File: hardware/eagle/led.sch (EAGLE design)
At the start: 15 parts, among them IC1 MCP1406SOIC8, IC10 MCP1406SOIC8, IC11 MCP1406SOIC8, IC12 MCP1406SOIC8, IC13 MCP2551SOIC8, IC2 MCP1406SOIC8, IC3 MCP1406SOIC8, IC4 MCP1406SOIC8, IC5 MCP1406SOIC8, IC6 MCP1406SOIC8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

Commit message: neue boaerd version + datasheets added
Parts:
- removed JP2: (no value), pinhead:PINHD-2X13
- added C2: (no value), rcl:CPOL-EUE5-10.5
- added EXT1: (no value), pinhead:PINHD-2X13
- added IC14: 7805T, linear:7805T
- added U$1, U$10, U$11, U$2, U$3, U$5, U$6, U$7, U$8, U$9: 2KLEMME, custom-parts:2KLEMME
- renumbered JP1 to EXT2
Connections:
- new net B1: EXT1.17, IC1.INPUT
- new net B2: EXT1.26, IC4.INPUT
- new net B3: EXT1.16, IC7.INPUT
- new net B4: EXT2.10, IC10.INPUT
- new net CANH: IC13.CANH, U$3.1
- new net CANL: IC13.CANL, U$3.2
- new net CANRX: EXT1.1, IC13.RXD
- new net CANTX: EXT1.3, IC13.TXD
- new net G1: EXT1.15, IC2.INPUT
- new net G2: EXT1.22, IC5.INPUT
- new net G3: EXT2.7, IC8.INPUT
- new net G4: EXT2.8, IC11.INPUT
- new net N$10: IC8.OUT1, IC8.OUT2, U$8.2
- new net N$11: IC7.OUT1, IC7.OUT2, U$7.1
- new net N$12: IC12.OUT1, IC12.OUT2, U$9.1
- new net N$13: IC11.OUT1, IC11.OUT2, U$9.2
- new net N$14: IC10.OUT1, IC10.OUT2, U$2.1
- new net N$2: C2.-, IC14.GND, U$1.2
- new net N$3: IC3.OUT1, IC3.OUT2, U$5.1
- new net N$4: IC2.OUT1, IC2.OUT2, U$5.2
- new net N$5: IC1.OUT1, IC1.OUT2, U$6.1
- new net N$6: IC6.OUT1, IC6.OUT2, U$10.1
- new net N$7: IC5.OUT1, IC5.OUT2, U$10.2
- new net N$8: IC4.OUT1, IC4.OUT2, U$11.1
- new net N$9: IC9.OUT1, IC9.OUT2, U$8.1
- new net R1: EXT1.13, IC3.INPUT
- new net R2: EXT1.21, IC6.INPUT
- new net R3: EXT1.14, IC9.INPUT
- new net R4: EXT2.4, IC12.INPUT
- new net VCC: EXT2.26, IC13.VDD, IC14.VO
- net +12V: now also C2.+, IC14.VI, U$1.1, U$2.2
- net GND: now also EXT2.25, IC13.GND, U$11.2, U$6.2, U$7.2

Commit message: hardware changed
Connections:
- net +12V: no longer U$2.2
- net B3: now also EXT1.14; no longer EXT1.16
- net G3: now also EXT1.16; no longer EXT2.7
- net GND: now also U$2.2
- net R3: now also EXT2.7; no longer EXT1.14
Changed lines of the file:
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@@
 <pinref part="GND5" gate="1" pin="GND"/>
 <wire x1="241.3" y1="55.88" x2="246.38" y2="55.88" width="0.1524" layer="91"/>
-<wire x1="246.38" y1="55.88" x2="246.38" y2="38.1" width="0.1524" layer="91"/>
+<wire x1="246.38" y1="55.88" x2="246.38" y2="50.8" width="0.1524" layer="91"/>
 <pinref part="IC10" gate="G$1" pin="GND2"/>
+<wire x1="246.38" y1="50.8" x2="246.38" y2="38.1" width="0.1524" layer="91"/>
 <wire x1="246.38" y1="38.1" x2="246.38" y2="20.32" width="0.1524" layer="91"/>
 <wire x1="246.38" y1="20.32" x2="246.38" y2="12.7" width="0.1524" layer="91"/>
@@
 <junction x="246.38" y="38.1"/>
 <junction x="246.38" y="55.88"/>
+<pinref part="U$2" gate="G$1" pin="2"/>
+<wire x1="279.4" y1="86.36" x2="279.4" y2="50.8" width="0.1524" layer="91"/>
+<wire x1="279.4" y1="50.8" x2="246.38" y2="50.8" width="0.1524" layer="91"/>
+<junction x="246.38" y="50.8"/>
 </segment>
 <segment>
@@
 <junction x="256.54" y="63.5"/>
 <junction x="256.54" y="27.94"/>
-<pinref part="U$2" gate="G$1" pin="2"/>
-<wire x1="279.4" y1="86.36" x2="279.4" y2="45.72" width="0.1524" layer="91"/>
-<wire x1="279.4" y1="45.72" x2="256.54" y2="45.72" width="0.1524" layer="91"/>
 </segment>
 <segment>
@@
 <pinref part="IC9" gate="G$1" pin="INPUT"/>
 <wire x1="144.78" y1="60.96" x2="142.24" y2="60.96" width="0.1524" layer="91"/>
-<label x="139.7" y="58.42" size="1.778" layer="95"/>
+<label x="137.16" y="60.96" size="1.778" layer="95"/>
+</segment>
+<segment>
+<pinref part="EXT2" gate="A" pin="7"/>
+<wire x1="353.06" y1="137.16" x2="342.9" y2="137.16" width="0.1524" layer="91"/>
+<label x="337.82" y="137.16" size="1.778" layer="95"/>
+</segment>
+</net>
+<net name="G3" class="0">
+<segment>
+<pinref part="IC8" gate="G$1" pin="INPUT"/>
+<wire x1="144.78" y1="43.18" x2="142.24" y2="43.18" width="0.1524" layer="91"/>
+<label x="134.62" y="43.18" size="1.778" layer="95"/>
+</segment>
+<segment>
+<pinref part="EXT1" gate="A" pin="16"/>
+<wire x1="302.26" y1="127" x2="312.42" y2="127" width="0.1524" layer="91"/>
+<label x="314.96" y="127" size="1.778" layer="95"/>
+</segment>
+</net>
+<net name="B3" class="0">
+<segment>
+<pinref part="IC7" gate="G$1" pin="INPUT"/>
+<wire x1="144.78" y1="25.4" x2="142.24" y2="25.4" width="0.1524" layer="91"/>
+<label x="134.62" y="25.4" size="1.778" layer="95"/>
 </segment>
 <segment>
@@
 </segment>
 </net>
-<net name="G3" class="0">
-<segment>
-<pinref part="IC8" gate="G$1" pin="INPUT"/>
-<wire x1="144.78" y1="43.18" x2="142.24" y2="43.18" width="0.1524" layer="91"/>
-<label x="132.08" y="40.64" size="1.778" layer="95"/>
-</segment>
-<segment>
-<pinref part="EXT2" gate="A" pin="7"/>
-<wire x1="353.06" y1="137.16" x2="342.9" y2="137.16" width="0.1524" layer="91"/>
-<label x="337.82" y="137.16" size="1.778" layer="95"/>
-</segment>
-</net>
-<net name="B3" class="0">
-<segment>
-<pinref part="IC7" gate="G$1" pin="INPUT"/>
-<wire x1="144.78" y1="25.4" x2="142.24" y2="25.4" width="0.1524" layer="91"/>
-<label x="134.62" y="22.86" size="1.778" layer="95"/>
-</segment>
-<segment>
-<pinref part="EXT1" gate="A" pin="16"/>
-<wire x1="302.26" y1="127" x2="312.42" y2="127" width="0.1524" layer="91"/>
-<label x="314.96" y="127" size="1.778" layer="95"/>
-</segment>
-</net>

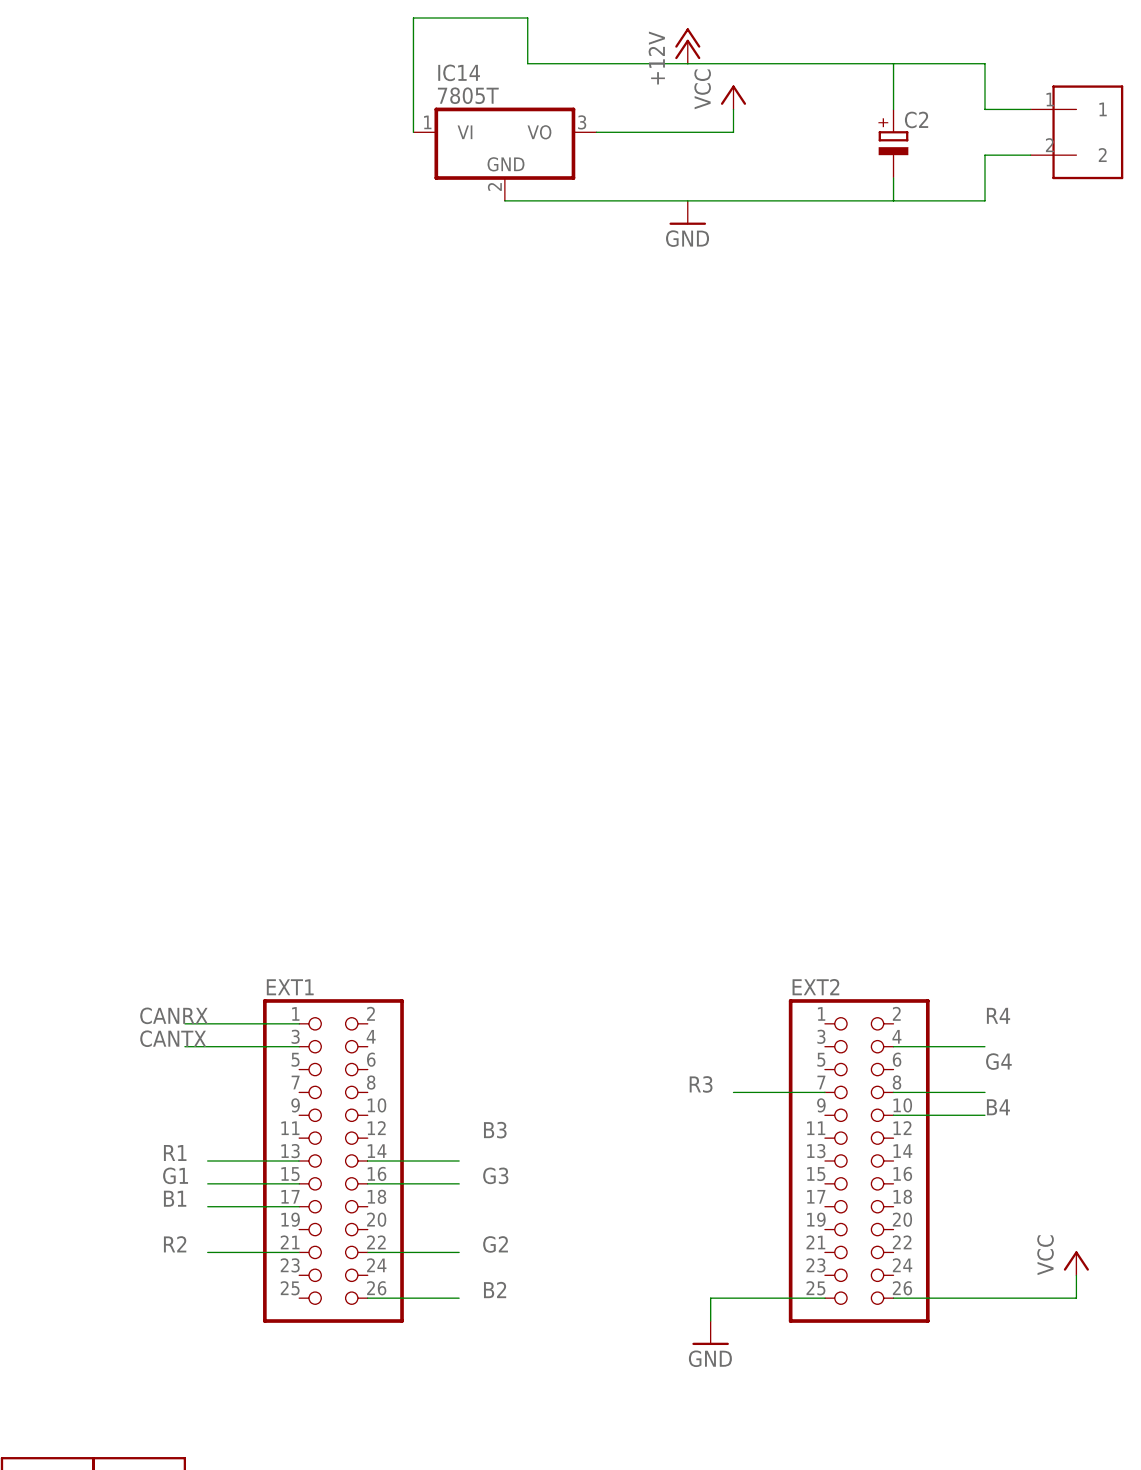
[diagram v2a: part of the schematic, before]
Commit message: neues board nicht fertig geroutet wegen kreuzungen
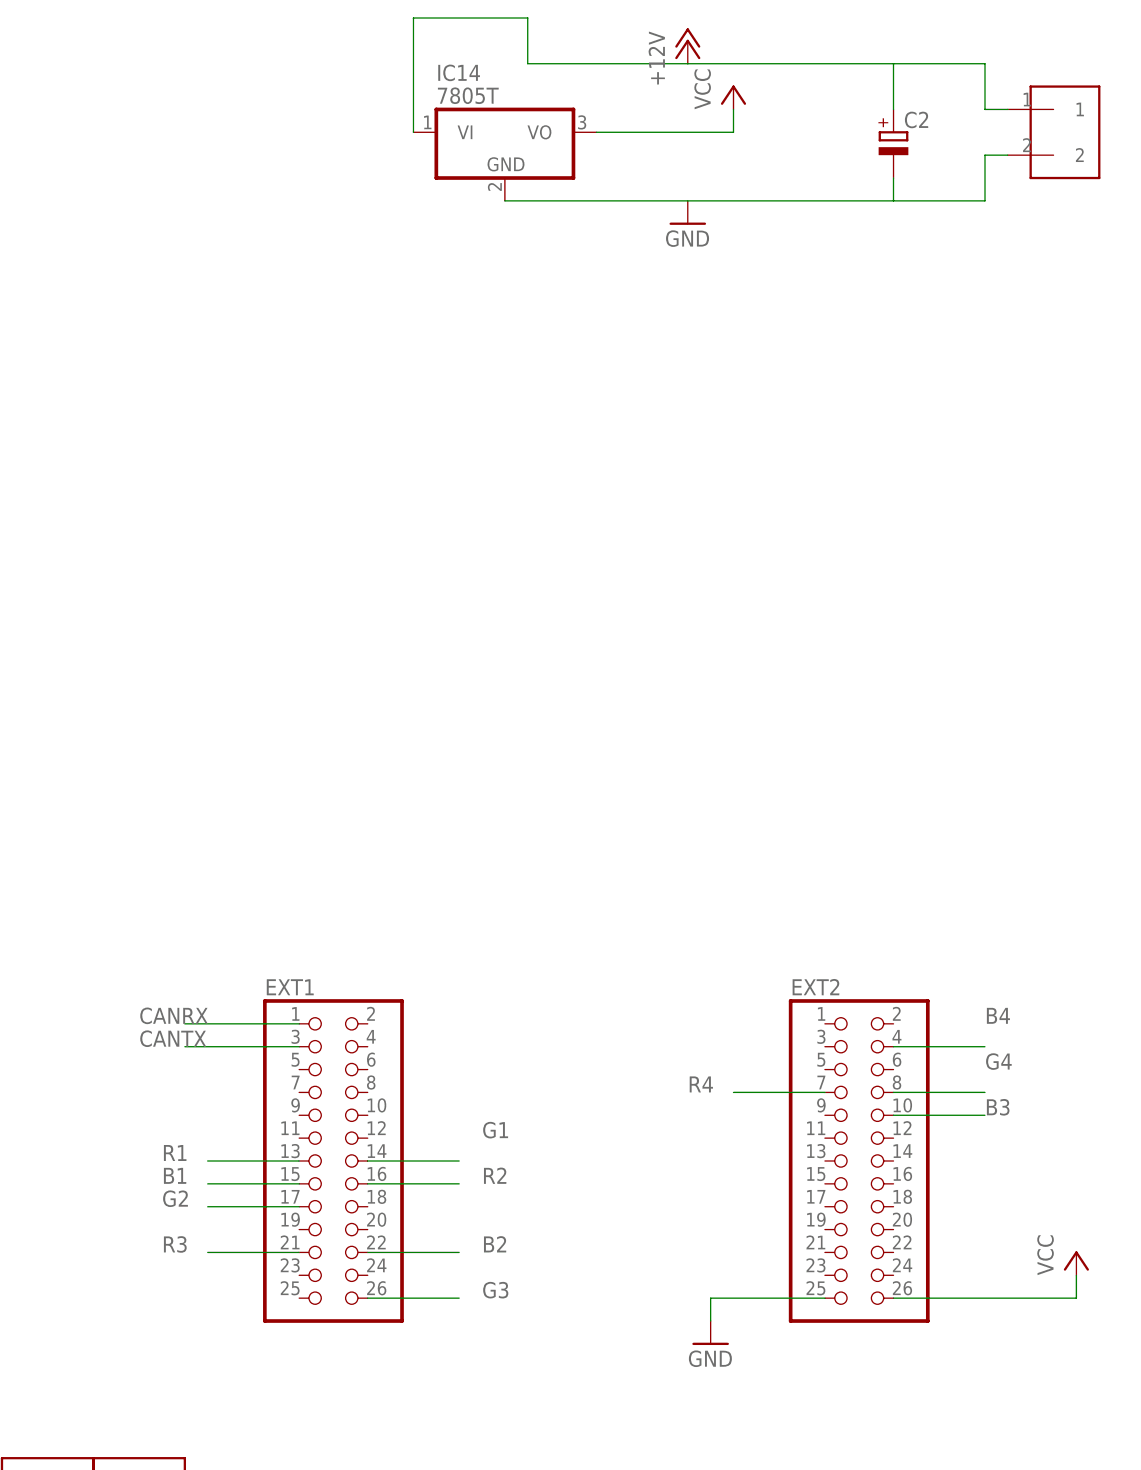
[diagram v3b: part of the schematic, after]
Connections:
- net B1: now also EXT1.15; no longer EXT1.17
- net B2: now also EXT1.22; no longer EXT1.26
- net B3: now also EXT2.10; no longer EXT1.14
- net B4: now also EXT2.4; no longer EXT2.10
- net G1: now also EXT1.14; no longer EXT1.15
- net G2: now also EXT1.17; no longer EXT1.22
- net G3: now also EXT1.26; no longer EXT1.16
- net R2: now also EXT1.16; no longer EXT1.21
- net R3: now also EXT1.21; no longer EXT2.7
- net R4: now also EXT2.7; no longer EXT2.4
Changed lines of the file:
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@@
 <instance part="P+6" gate="1" x="337.82" y="254"/>
 <instance part="GND6" gate="1" x="337.82" y="233.68"/>
-<instance part="U$1" gate="G$1" x="383.54" y="243.84"/>
+<instance part="U$1" gate="G$1" x="381" y="243.84"/>
 <instance part="U$2" gate="G$1" x="276.86" y="93.98" rot="R90"/>
 <instance part="U$5" gate="G$1" x="60.96" y="93.98" rot="R90"/>
@@
 <wire x1="360.68" y1="251.46" x2="370.84" y2="251.46" width="0.1524" layer="91"/>
 <wire x1="360.68" y1="251.46" x2="360.68" y2="246.38" width="0.1524" layer="91"/>
-<pinref part="U$1" gate="G$1" pin="1"/>
-<wire x1="375.92" y1="246.38" x2="370.84" y2="246.38" width="0.1524" layer="91"/>
 <wire x1="370.84" y1="246.38" x2="370.84" y2="251.46" width="0.1524" layer="91"/>
 <wire x1="337.82" y1="251.46" x2="320.04" y2="251.46" width="0.1524" layer="91"/>
@@
 <wire x1="320.04" y1="256.54" x2="307.34" y2="256.54" width="0.1524" layer="91"/>
 <wire x1="307.34" y1="256.54" x2="307.34" y2="243.84" width="0.1524" layer="91"/>
+<pinref part="U$1" gate="G$1" pin="1"/>
+<wire x1="373.38" y1="246.38" x2="370.84" y2="246.38" width="0.1524" layer="91"/>
 </segment>
 </net>
@@
 <wire x1="360.68" y1="236.22" x2="370.84" y2="236.22" width="0.1524" layer="91"/>
 <wire x1="360.68" y1="238.76" x2="360.68" y2="236.22" width="0.1524" layer="91"/>
-<pinref part="U$1" gate="G$1" pin="2"/>
-<wire x1="375.92" y1="241.3" x2="370.84" y2="241.3" width="0.1524" layer="91"/>
 <wire x1="370.84" y1="241.3" x2="370.84" y2="236.22" width="0.1524" layer="91"/>
 <pinref part="IC14" gate="A1" pin="GND"/>
+<pinref part="U$1" gate="G$1" pin="2"/>
+<wire x1="373.38" y1="241.3" x2="370.84" y2="241.3" width="0.1524" layer="91"/>
 </segment>
 </net>
@@
 </segment>
 <segment>
+<pinref part="EXT1" gate="A" pin="14"/>
+<wire x1="302.26" y1="129.54" x2="312.42" y2="129.54" width="0.1524" layer="91"/>
+<label x="314.96" y="132.08" size="1.778" layer="95"/>
+</segment>
+</net>
+<net name="B1" class="0">
+<segment>
+<pinref part="IC1" gate="G$1" pin="INPUT"/>
+<wire x1="22.86" y1="25.4" x2="20.32" y2="25.4" width="0.1524" layer="91"/>
+<label x="10.16" y="22.86" size="1.778" layer="95"/>
+</segment>
+<segment>
 <pinref part="EXT1" gate="A" pin="15"/>
 <wire x1="294.64" y1="127" x2="284.48" y2="127" width="0.1524" layer="91"/>
@@
 </segment>
 </net>
-<net name="B1" class="0">
-<segment>
-<pinref part="IC1" gate="G$1" pin="INPUT"/>
-<wire x1="22.86" y1="25.4" x2="20.32" y2="25.4" width="0.1524" layer="91"/>
-<label x="10.16" y="22.86" size="1.778" layer="95"/>
+<net name="B2" class="0">
+<segment>
+<pinref part="IC4" gate="G$1" pin="INPUT"/>
+<wire x1="83.82" y1="25.4" x2="81.28" y2="25.4" width="0.1524" layer="91"/>
+<label x="71.12" y="22.86" size="1.778" layer="95"/>
+</segment>
+<segment>
+<pinref part="EXT1" gate="A" pin="22"/>
+<wire x1="302.26" y1="119.38" x2="312.42" y2="119.38" width="0.1524" layer="91"/>
+<label x="314.96" y="119.38" size="1.778" layer="95"/>
+</segment>
+</net>
+<net name="G2" class="0">
+<segment>
+<pinref part="IC5" gate="G$1" pin="INPUT"/>
+<wire x1="83.82" y1="43.18" x2="81.28" y2="43.18" width="0.1524" layer="91"/>
+<label x="71.12" y="40.64" size="1.778" layer="95"/>
 </segment>
 <segment>
@@
 </segment>
 </net>
-<net name="B2" class="0">
-<segment>
-<pinref part="IC4" gate="G$1" pin="INPUT"/>
-<wire x1="83.82" y1="25.4" x2="81.28" y2="25.4" width="0.1524" layer="91"/>
-<label x="71.12" y="22.86" size="1.778" layer="95"/>
+<net name="R3" class="0">
+<segment>
+<pinref part="IC9" gate="G$1" pin="INPUT"/>
+<wire x1="144.78" y1="60.96" x2="142.24" y2="60.96" width="0.1524" layer="91"/>
+<label x="137.16" y="60.96" size="1.778" layer="95"/>
+</segment>
+<segment>
+<pinref part="EXT1" gate="A" pin="21"/>
+<wire x1="294.64" y1="119.38" x2="284.48" y2="119.38" width="0.1524" layer="91"/>
+<label x="279.4" y="119.38" size="1.778" layer="95"/>
+</segment>
+</net>
+<net name="G3" class="0">
+<segment>
+<pinref part="IC8" gate="G$1" pin="INPUT"/>
+<wire x1="144.78" y1="43.18" x2="142.24" y2="43.18" width="0.1524" layer="91"/>
+<label x="134.62" y="43.18" size="1.778" layer="95"/>
 </segment>
 <segment>
@@
 </segment>
 </net>
-<net name="G2" class="0">
-<segment>
-<pinref part="IC5" gate="G$1" pin="INPUT"/>
-<wire x1="83.82" y1="43.18" x2="81.28" y2="43.18" width="0.1524" layer="91"/>
-<label x="71.12" y="40.64" size="1.778" layer="95"/>
-</segment>
-<segment>
-<pinref part="EXT1" gate="A" pin="22"/>
-<wire x1="302.26" y1="119.38" x2="312.42" y2="119.38" width="0.1524" layer="91"/>
-<label x="314.96" y="119.38" size="1.778" layer="95"/>
-</segment>
-</net>
-<net name="R3" class="0">
-<segment>
-<pinref part="IC9" gate="G$1" pin="INPUT"/>
-<wire x1="144.78" y1="60.96" x2="142.24" y2="60.96" width="0.1524" layer="91"/>
-<label x="137.16" y="60.96" size="1.778" layer="95"/>
+<net name="B3" class="0">
+<segment>
+<pinref part="IC7" gate="G$1" pin="INPUT"/>
+<wire x1="144.78" y1="25.4" x2="142.24" y2="25.4" width="0.1524" layer="91"/>
+<label x="134.62" y="25.4" size="1.778" layer="95"/>
+</segment>
+<segment>
+<pinref part="EXT2" gate="A" pin="10"/>
+<wire x1="360.68" y1="134.62" x2="370.84" y2="134.62" width="0.1524" layer="91"/>
+<label x="370.84" y="134.62" size="1.778" layer="95"/>
+</segment>
+</net>
+<net name="B4" class="0">
+<segment>
+<pinref part="IC10" gate="G$1" pin="INPUT"/>
+<wire x1="210.82" y1="25.4" x2="208.28" y2="25.4" width="0.1524" layer="91"/>
+<label x="198.12" y="22.86" size="1.778" layer="95"/>
+</segment>
+<segment>
+<pinref part="EXT2" gate="A" pin="4"/>
+<wire x1="360.68" y1="142.24" x2="370.84" y2="142.24" width="0.1524" layer="91"/>
+<label x="370.84" y="144.78" size="1.778" layer="95"/>
+</segment>
+</net>
+<net name="G4" class="0">
+<segment>
+<pinref part="IC11" gate="G$1" pin="INPUT"/>
+<wire x1="210.82" y1="43.18" x2="208.28" y2="43.18" width="0.1524" layer="91"/>
+<label x="198.12" y="40.64" size="1.778" layer="95"/>
+</segment>
+<segment>
+<pinref part="EXT2" gate="A" pin="8"/>
+<wire x1="360.68" y1="137.16" x2="370.84" y2="137.16" width="0.1524" layer="91"/>
+<label x="370.84" y="139.7" size="1.778" layer="95"/>
+</segment>
+</net>
+<net name="R4" class="0">
+<segment>
+<pinref part="IC12" gate="G$1" pin="INPUT"/>
+<wire x1="210.82" y1="60.96" x2="208.28" y2="60.96" width="0.1524" layer="91"/>
+<label x="203.2" y="58.42" size="1.778" layer="95"/>
 </segment>
 <segment>
@@
 </segment>
 </net>
-<net name="G3" class="0">
-<segment>
-<pinref part="IC8" gate="G$1" pin="INPUT"/>
-<wire x1="144.78" y1="43.18" x2="142.24" y2="43.18" width="0.1524" layer="91"/>
-<label x="134.62" y="43.18" size="1.778" layer="95"/>
+<net name="R2" class="0">
+<segment>
+<pinref part="IC6" gate="G$1" pin="INPUT"/>
+<wire x1="83.82" y1="60.96" x2="81.28" y2="60.96" width="0.1524" layer="91"/>
+<label x="76.2" y="58.42" size="1.778" layer="95"/>
 </segment>
 <segment>
@@
 </segment>
 </net>
-<net name="B3" class="0">
-<segment>
-<pinref part="IC7" gate="G$1" pin="INPUT"/>
-<wire x1="144.78" y1="25.4" x2="142.24" y2="25.4" width="0.1524" layer="91"/>
-<label x="134.62" y="25.4" size="1.778" layer="95"/>
-</segment>
-<segment>
-<pinref part="EXT1" gate="A" pin="14"/>
-<wire x1="302.26" y1="129.54" x2="312.42" y2="129.54" width="0.1524" layer="91"/>
-<label x="314.96" y="132.08" size="1.778" layer="95"/>
-</segment>
-</net>
-<net name="B4" class="0">
-<segment>
-<pinref part="IC10" gate="G$1" pin="INPUT"/>
-<wire x1="210.82" y1="25.4" x2="208.28" y2="25.4" width="0.1524" layer="91"/>
-<label x="198.12" y="22.86" size="1.778" layer="95"/>
-</segment>
-<segment>
-<pinref part="EXT2" gate="A" pin="10"/>
-<wire x1="360.68" y1="134.62" x2="370.84" y2="134.62" width="0.1524" layer="91"/>
-<label x="370.84" y="134.62" size="1.778" layer="95"/>
-</segment>
-</net>
-<net name="G4" class="0">
-<segment>
-<pinref part="IC11" gate="G$1" pin="INPUT"/>
-<wire x1="210.82" y1="43.18" x2="208.28" y2="43.18" width="0.1524" layer="91"/>
-<label x="198.12" y="40.64" size="1.778" layer="95"/>
-</segment>
-<segment>
-<pinref part="EXT2" gate="A" pin="8"/>
-<wire x1="360.68" y1="137.16" x2="370.84" y2="137.16" width="0.1524" layer="91"/>
-<label x="370.84" y="139.7" size="1.778" layer="95"/>
-</segment>
-</net>
-<net name="R4" class="0">
-<segment>
-<pinref part="IC12" gate="G$1" pin="INPUT"/>
-<wire x1="210.82" y1="60.96" x2="208.28" y2="60.96" width="0.1524" layer="91"/>
-<label x="203.2" y="58.42" size="1.778" layer="95"/>
-</segment>
-<segment>
-<pinref part="EXT2" gate="A" pin="4"/>
-<wire x1="360.68" y1="142.24" x2="370.84" y2="142.24" width="0.1524" layer="91"/>
-<label x="370.84" y="144.78" size="1.778" layer="95"/>
-</segment>
-</net>
-<net name="R2" class="0">
-<segment>
-<pinref part="IC6" gate="G$1" pin="INPUT"/>
-<wire x1="83.82" y1="60.96" x2="81.28" y2="60.96" width="0.1524" layer="91"/>
-<label x="76.2" y="58.42" size="1.778" layer="95"/>
-</segment>
-<segment>
-<pinref part="EXT1" gate="A" pin="21"/>
-<wire x1="294.64" y1="119.38" x2="284.48" y2="119.38" width="0.1524" layer="91"/>
-<label x="279.4" y="119.38" size="1.778" layer="95"/>
-</segment>
-</net>

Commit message: einige datein mal mit commitet da die sonst immer vergessen wurden
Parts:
- removed IC14: 7805T, linear:7805T
- added C1, C3: 10nF, rcl:C-EU025-025X050
- added D1, D2, D3, D9: 1N4001, diode:DIODE-MELF-MLL41
- added F2: FUSESH35, fuse:FUSESH35
- added IC15: 7805TV, linear:7805TV
- added JP3: LEDS, pinhead:PINHD-1X4
- added R1, R2, R3: 280R, rcl:R-EU_0204/7
- C2: value (none) -> 1000µF; device rcl:CPOL-EUE5-10.5 -> rcl:CPOL-EUE5-8.5
- U$3: value 2KLEMME -> 3KLEMME; device custom-parts:2KLEMME -> custom-parts:3KLEMME
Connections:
- removed net VCC: EXT2.26, IC13.VDD, IC14.VO
- new net +5V: C1.1, D9.A, EXT2.26, IC13.VDD, IC15.VO
- new net LED1: EXT2.20, R1.2
- new net LED2: EXT2.21, R2.2
- new net LED3: EXT2.22, R3.2
- new net N$1: C3.1, D1.C, D9.C, IC15.VI
- new net N$32: JP3.1, R1.1
- new net N$36: JP3.2, R2.1
- new net N$37: JP3.3, R3.1
- net +12V: now also D1.A, D2.C, D3.C, U$1.2; no longer IC14.VI, U$1.1
- net GND: now also C1.2, C2.-, C3.2, D2.A, D3.A, F2.2, IC13.RS, IC15.GND, IC8.GND1, JP3.4, U$3.3
- net N$2: now also F2.1, U$1.1; no longer C2.-, IC14.GND, U$1.2
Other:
- moved on the sheet: C2
